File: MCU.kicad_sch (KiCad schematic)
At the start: 41 parts, among them IC8 ATSAMD21G18A-MF, J10 Conn_01x06, J7 Conn_01x08, J8 Conn_01x10, J9 Conn_01x08, Q1 XTAL_32.768KHZ_ABRACON_ABS09-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

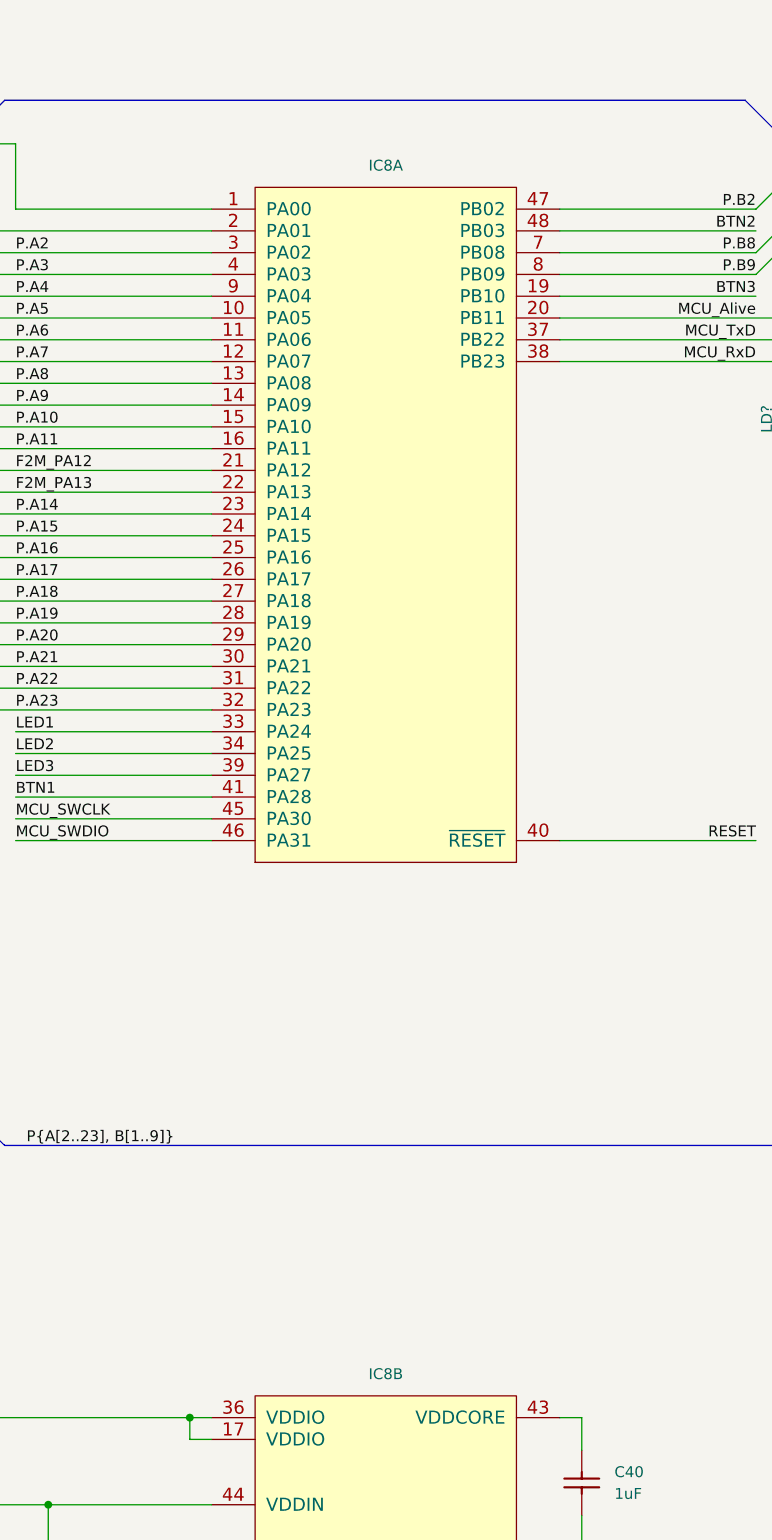
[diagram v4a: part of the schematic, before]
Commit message: Switched to iCE5LP4K, added power switch and 3V ref
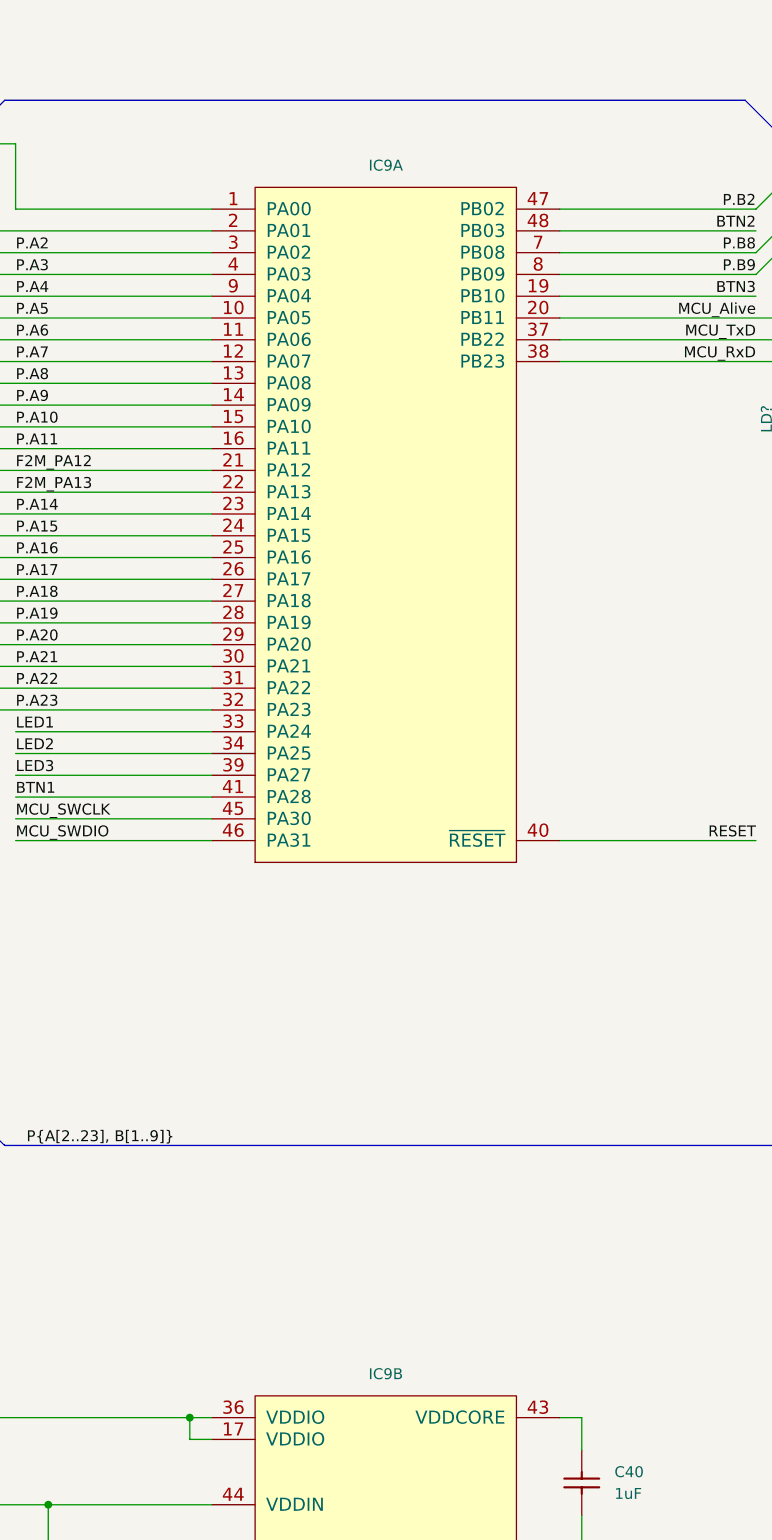
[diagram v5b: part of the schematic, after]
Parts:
- renumbered IC8 to IC9
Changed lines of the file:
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@@
   (symbol (lib_id "Logic:ATSAMD21G18A-MF") (at 143.51 53.34 0) (unit 1)
     (in_bom yes) (on_board yes) (dnp no) (fields_autoplaced)
-    (property "Reference" "IC8" (at 158.75 50.8 0)
+    (property "Reference" "IC9" (at 158.75 50.8 0)
       (effects (font (size 1.27 1.27)))
     )
@@
       (project "Accurate_Eval"
         (path "/d3b6a045-fd77-42ad-b330-1b1925488537/c6a8b2ea-c0f0-4c02-aeaa-57ac874f0dd5"
-          (reference "IC8") (unit 1)
+          (reference "IC9") (unit 1)
         )
       )
@@
   (symbol (lib_id "Logic:ATSAMD21G18A-MF") (at 143.51 194.31 0) (unit 2)
     (in_bom yes) (on_board yes) (dnp no) (fields_autoplaced)
-    (property "Reference" "IC8" (at 158.75 191.77 0)
+    (property "Reference" "IC9" (at 158.75 191.77 0)
       (effects (font (size 1.27 1.27)))
     )
@@
       (project "Accurate_Eval"
         (path "/d3b6a045-fd77-42ad-b330-1b1925488537/c6a8b2ea-c0f0-4c02-aeaa-57ac874f0dd5"
-          (reference "IC8") (unit 2)
-        )
-      )
+          (reference "IC9") (unit 2)
+        )
+      )

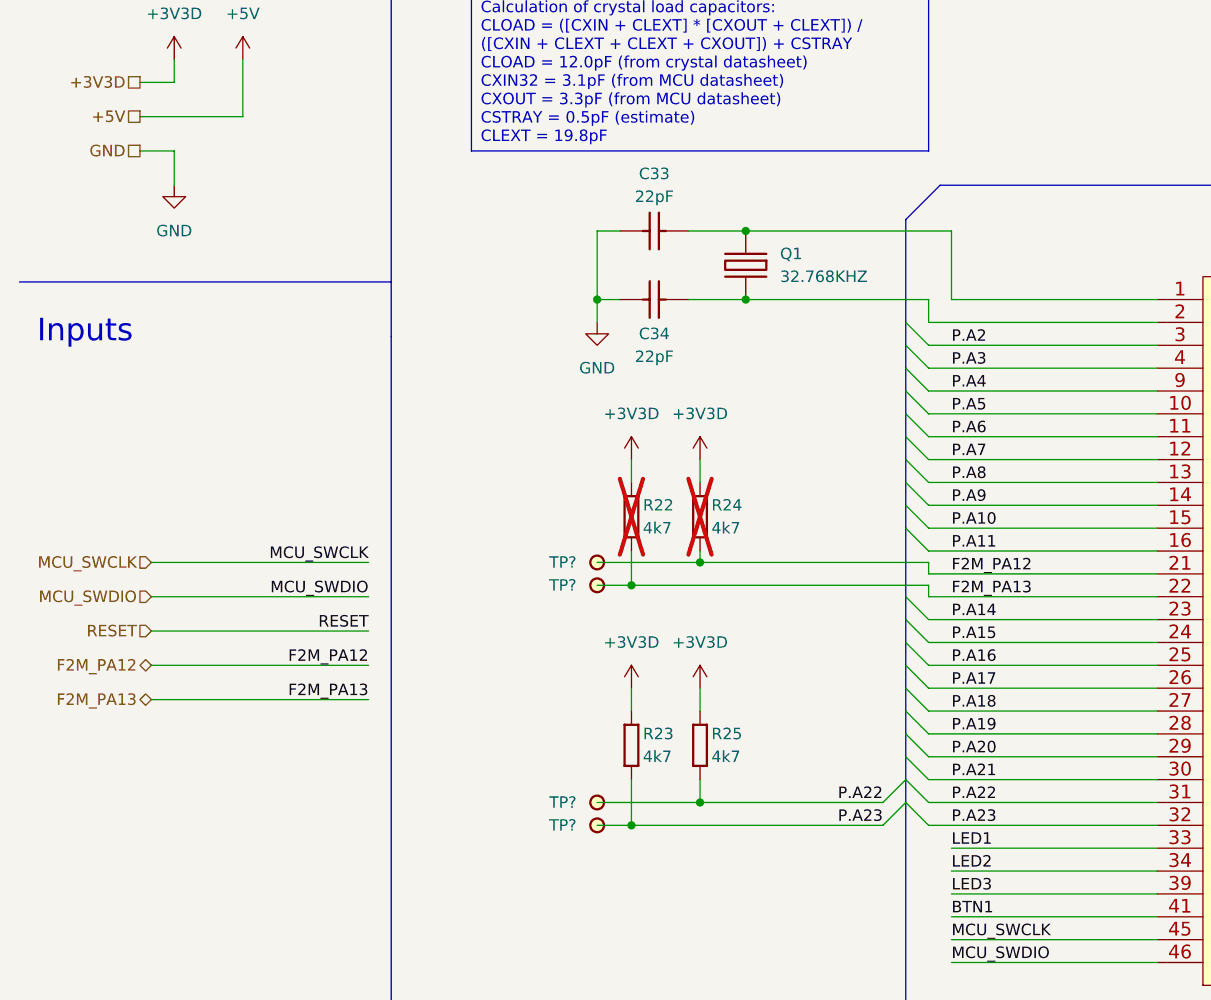
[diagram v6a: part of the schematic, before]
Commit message: Made more descriptive labels and titles
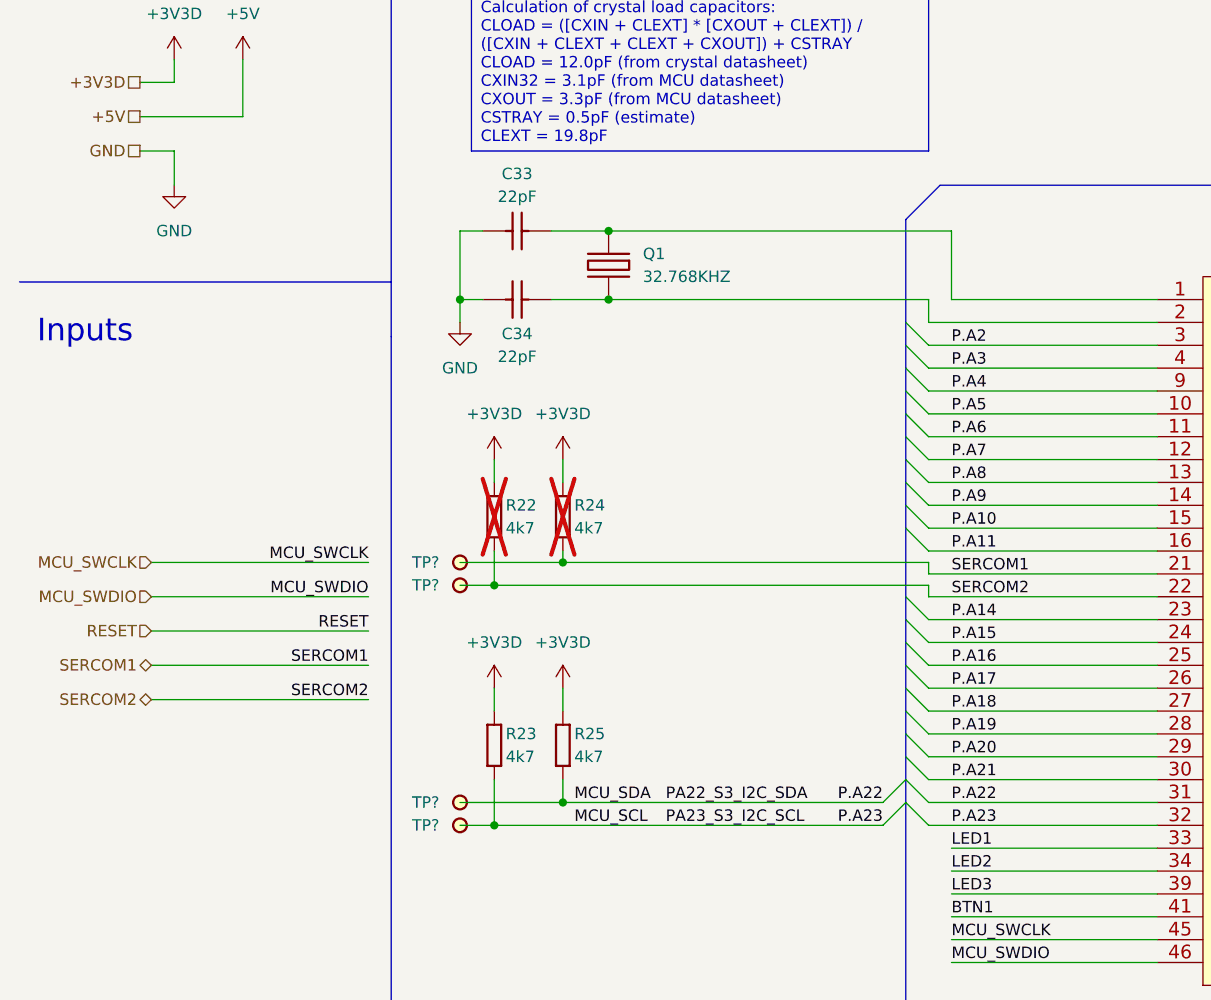
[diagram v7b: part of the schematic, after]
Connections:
- net F2M_PA12 renamed SERCOM1
- net F2M_PA13 renamed SERCOM2
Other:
- moved on the sheet: C33, C34, Q1, R22, R23, R24, R25, TP?

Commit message: Fixed comments after schematics review from Clyde
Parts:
- removed LD? (x2): LED_LITEON_LTST-C193KSKT-5A, ICs And Semiconductors SMD:LED_LITEON_LTST-C193KSKT-5A, symbol LEDs & Displays:LED_LITEON_LTST-C193KSKT-5A
- removed LD?: LED_LITEON_LTST-C193KGKT-5A, ICs And Semiconductors SMD:LED_LITEON_LTST-C193KGKT-5A, symbol LEDs & Displays:LED_LITEON_LTST-C193KGKT-5A
- removed R?: R0603_1K0_0.1%_0.063W_10PPM, Resistors SMD:RESC1608X55N, symbol Resistors SMD:R0603_1K0_0.1%_0.063W_10PPM
- added LD?: LED_LITEON_LTST-C193KGKT-5A, ICs And Semiconductors SMD:LED_LITEON_LTST-C193KGKT-5A, symbol LEDs & Displays:LED_LITEON_LTST-C193KGKT-5A
- added LD? (x2): LED_LITEON_LTST-C193KSKT-5A, ICs And Semiconductors SMD:LED_LITEON_LTST-C193KSKT-5A, symbol LEDs & Displays:LED_LITEON_LTST-C193KSKT-5A
- added R26: R0603_470R_1%_0.1W_100PPM, Resistors SMD:RESC1608X55N, symbol Resistors SMD:R0603_470R_1%_0.1W_100PPM
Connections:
- net +3V3D: now also LD?.2 (A), LD?.2 (A); no longer R27.1, R28.1
- net BTN3: now also IC9.37 (PB22); no longer IC9.19 (PB10)
- net GND: now also R26.2
- net MCU_Alive: now also IC9.38 (PB23), LD?.2 (A); no longer IC9.20 (PB11)
- net MCU_RxD: now also IC9.20 (PB11), R28.2; no longer IC9.38 (PB23)
- net MCU_TxD: now also IC9.19 (PB10), R27.2; no longer IC9.37 (PB22)
- new net: LD?.1 (C), R27.1
- new net: LD?.1 (C), R26.1
- new net: LD?.1 (C), R28.1
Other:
- moved on the sheet: C33, C34, Q1, R22, R23, R24, R25, TP?
